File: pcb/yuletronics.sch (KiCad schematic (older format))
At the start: 69 parts, among them IC1 STM32F042F6P6, IC2 MCP1700, IC3 TLV61220, J1 BATT, J2 MICROUSB, P1 SWD_TC, Q1 BSS138P, Q2 BSS138P, Q3 BSS138P, Q4 BSS138P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

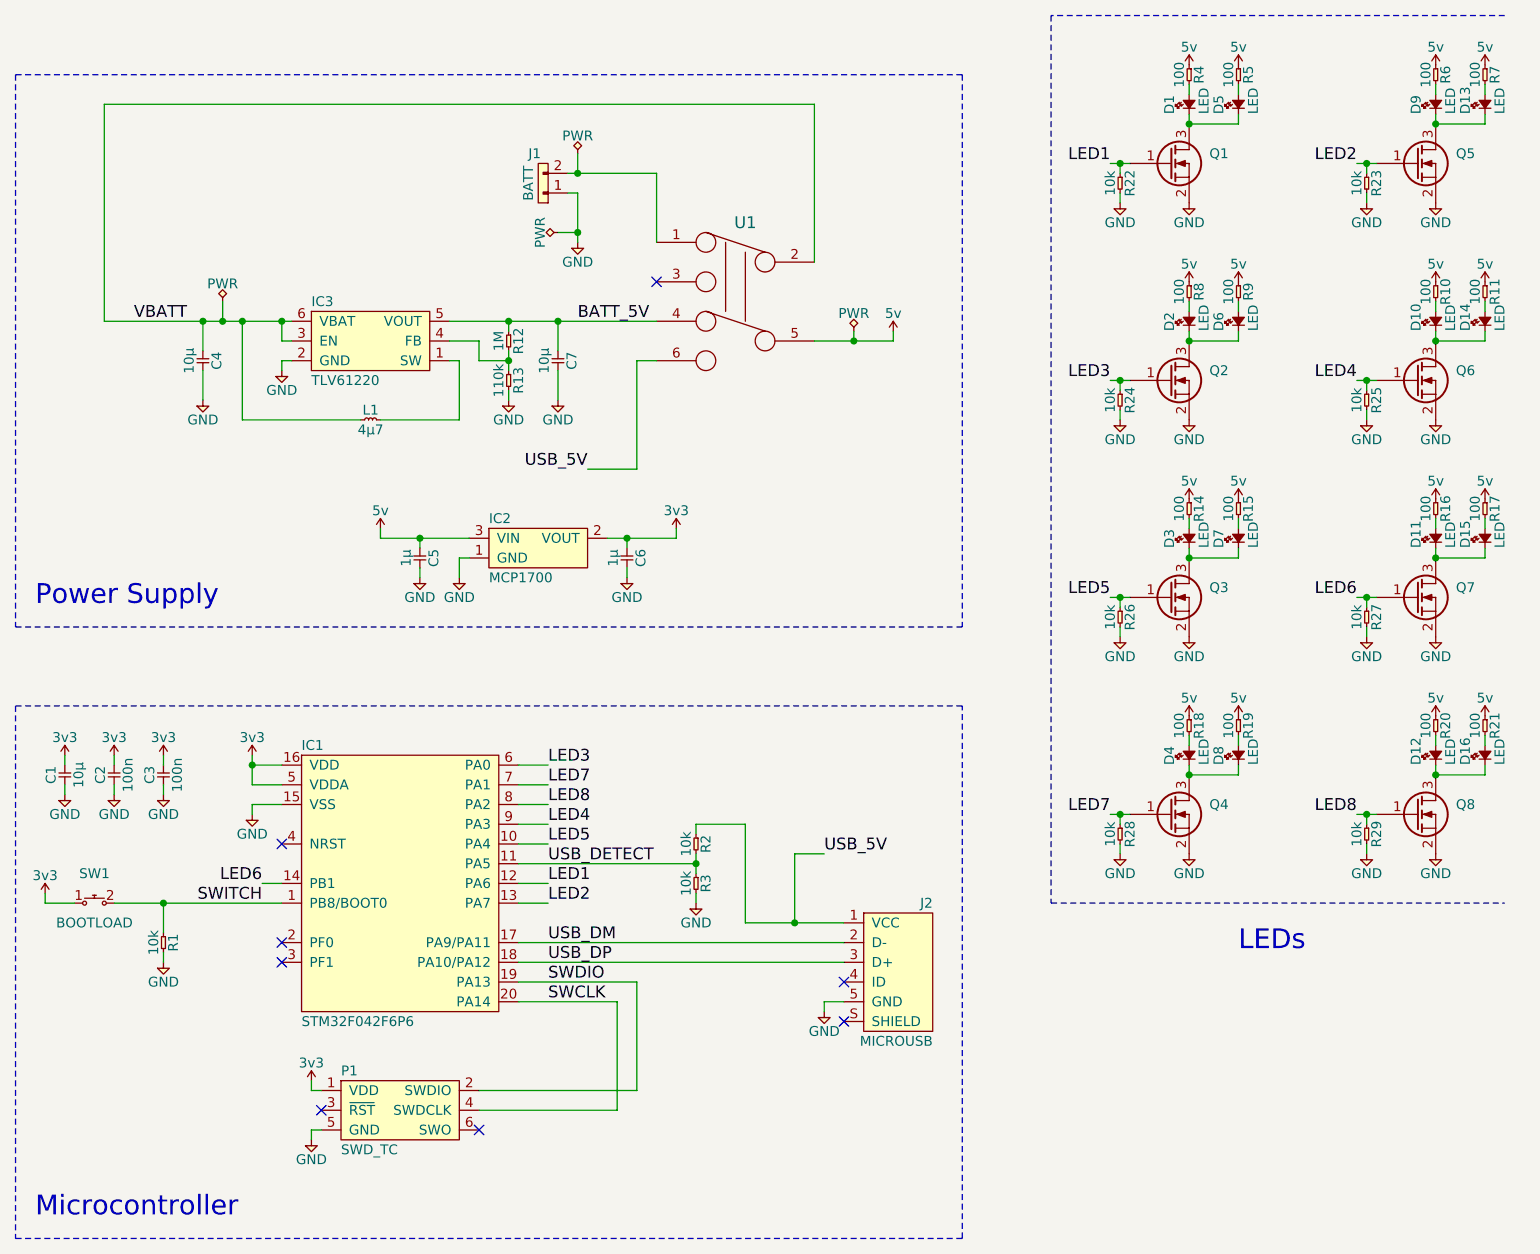
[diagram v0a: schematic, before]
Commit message: Removed switches and USB
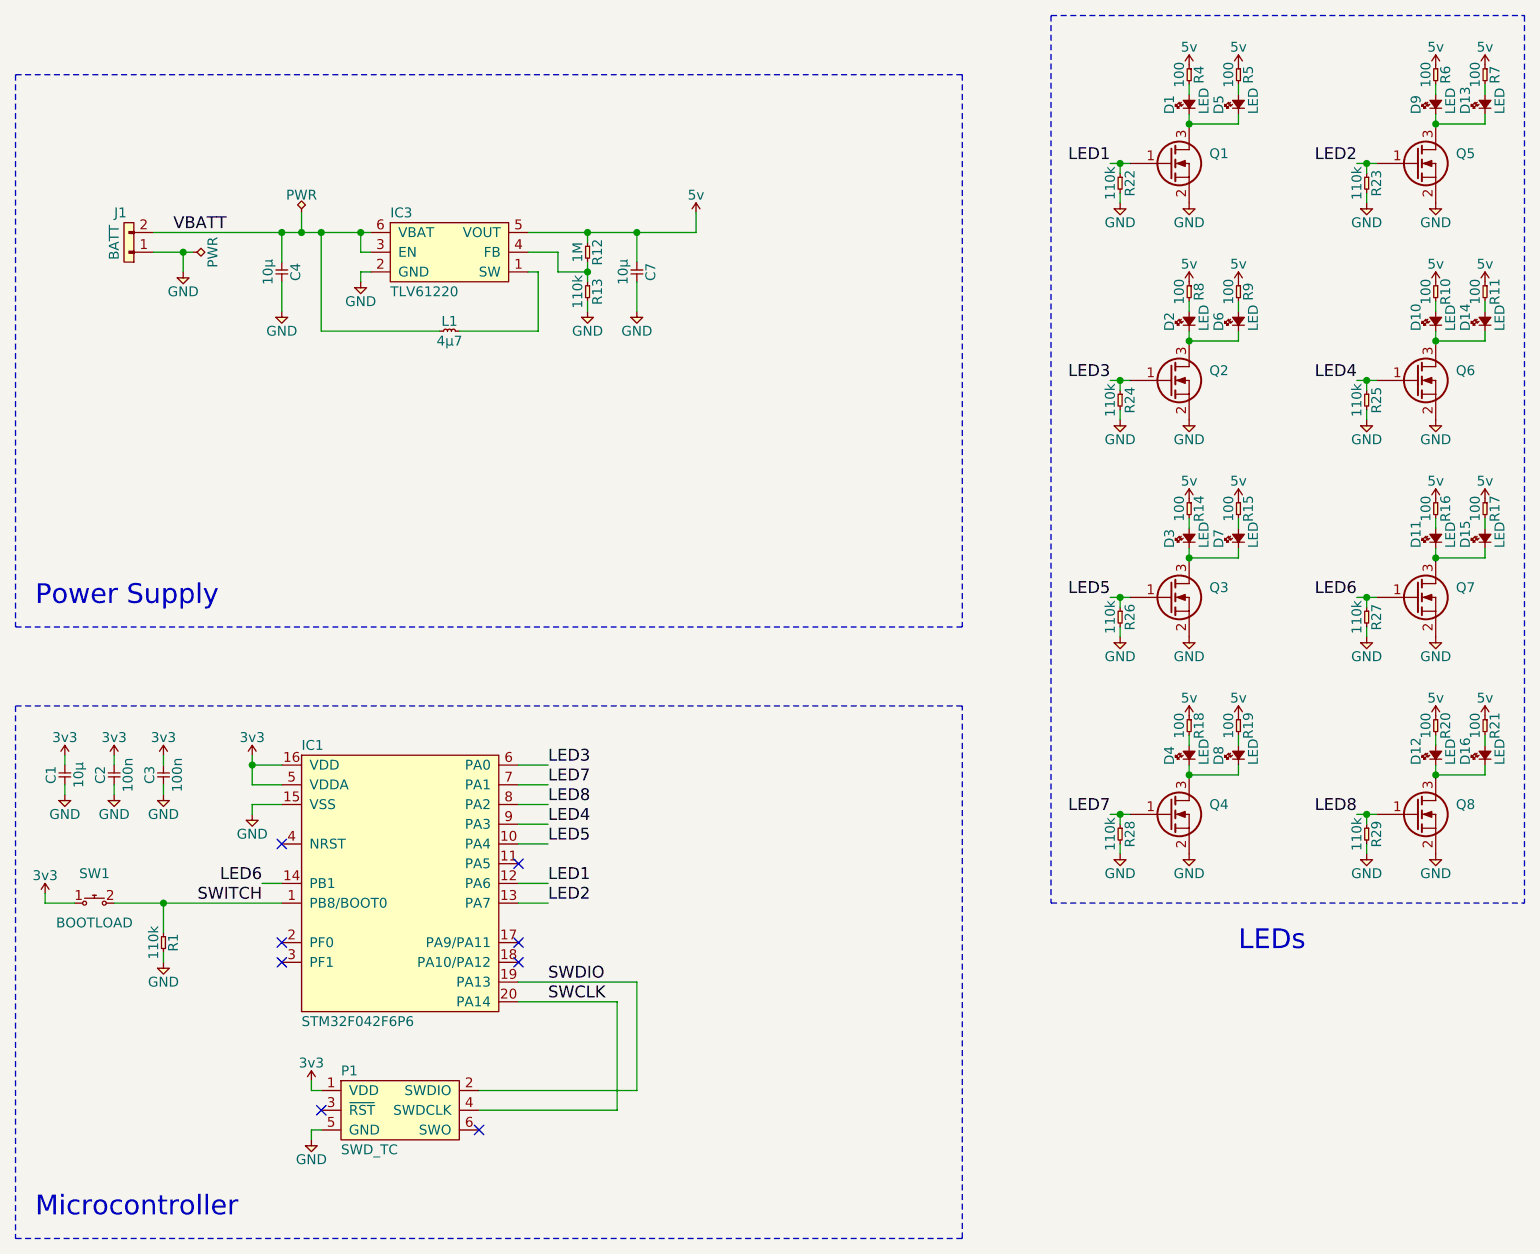
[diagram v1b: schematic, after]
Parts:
- removed C5, C6: 1µ, agg:0805, symbol C
- removed IC2: MCP1700, agg:SOT-23, symbol MCP1700
- removed J2: MICROUSB, agg:MICROUSB_MOLEX_47589-0001, symbol MICROUSB
- removed R2, R3: 10k, agg:0805, symbol R
- removed U1: dpdt, agg:dpdt, symbol dpdt
- R1: value 10k -> 110k; Farnell 9332391 -> 9332464
- R22, R23, R24, R25, R26, R27, R28, R29: value 10k -> 110k; Farnell (none) -> 9332464
- SW1: footprint agg:MOM_SWITCH -> agg:0805; Farnell 2056809 -> (none)
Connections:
- net BATT_5V is gone; now on net 5v: C7.1, IC3.5 (VOUT), R12.1
- net VBATT: now also J1.2
- net USB_DETECT: no longer names the net of IC1.11 (PA5)
- net USB_DM: no longer names the net of IC1.17 (PA9/PA11)
- net USB_DP: no longer names the net of IC1.18 (PA10/PA12)
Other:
- moved on the sheet: C4, C7, IC3, J1, L1, R12, R13

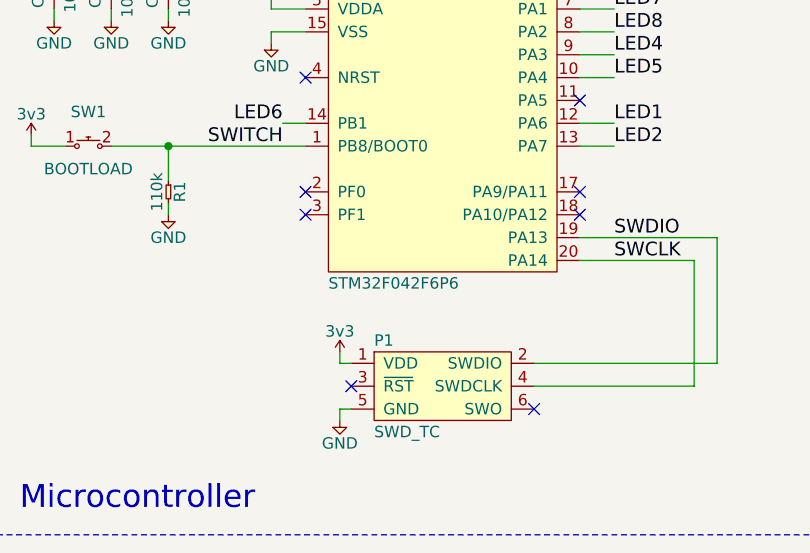
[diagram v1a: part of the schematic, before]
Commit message: Changed uc to STM32F030F4 TSSOP20
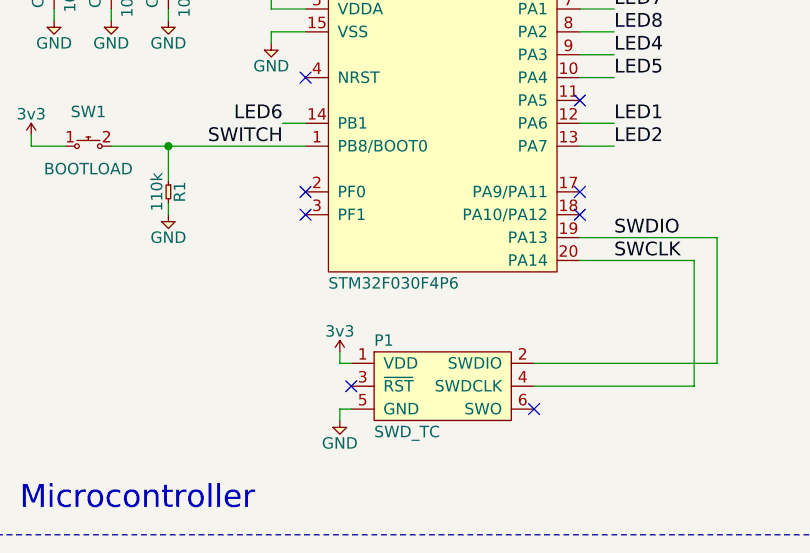
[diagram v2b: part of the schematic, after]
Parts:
- IC1: value STM32F042F6P6 -> STM32F030F4P6; Farnell 2469549 -> (none); RS (none) -> 792-5925
